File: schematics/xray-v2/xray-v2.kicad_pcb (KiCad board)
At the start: 4 copper layers, 144 x 69 mm, 136 parts, among them J1 USB_B_Micro, J2 USB_A, J3 USB_C_Receptacle_USB2.0, J4 USBASP, J5 USB_B_Micro, M1 VibroMotor, 3V, 8x2.7mm, Q1 IRF7832PbF, Q10 IRLML5203, Q11 IRLML0030, Q12 IRLML0030, Q13 IRLML0030, Q14 IRLML0030, Q2 IRF7425PbF, Q3 IRLML0030, Q4 IRF7425PbF, Q5 IRLML5203, Q6 IRLML5203, Q7 BC847, Q8 IRLML0030, Q9 IRLML5203, SW1 EC11W****, SW2 B3F3150, SW3 SW_Push, T1 Transformer_1P_1S, U1 PCA9306, U2 IP5328P, U3 ATmega328P-A, U4 SN74LVC2T45DCUR, U5 SN74LVC2T45DCUR, U6 SN74LVC2T45DCUR, U7 Display_1.18inch_st7535, U8 AMS1117-3.3, U9 CP2102N-Axx-xQFN28, Y1 HC-49SM, 8MHz

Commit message: Display changed 1.8'' -> 2.2''
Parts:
- D3, JP1, R17, SW3: moved to B.Cu
- U7: value Display_1.18inch_st7535 -> Display_2.2inch_ili9341; footprint Library:Display_1.18inch_st7735 -> Library:Display_2.2inch_ili9341
- moved H7 24.7 mm to (85.6, 50.5)
- moved D3 11.9 mm to (142.6, 75.3)
- moved U7 7.64 mm to (100.1, 134.2)
- moved R17 0.91 mm to (121.4, 67.3)
- moved JP1 0.81 mm to (128.6, 68.1), turned to -90 degrees
- moved SW3 0.46 mm to (114.2, 67.9), turned to 90 degrees
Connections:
- U7 pad 1: GND -> Net-(Q10-D)
- U7 pad 2: Net-(Q10-D) -> GND
- U7 pad 3: TFT_DC -> GND
- U7 pad 4: MOSI -> Net-(Q10-D)
- U7 pad 5: SCK -> TFT_DC
- U7 pad 6: unconnected-(U7-NC-Pad6) -> MOSI
- U7 pad 7: unconnected-(U7-NC-Pad7) -> SCK
- U7 pad 8: unconnected-(U7-NC-Pad8) -> Net-(Q10-D)
- U7 pad 9: GND -> MISO
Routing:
- net MISO: track 6.86 -> 48.9 mm
- net Net-(Q10-D): track 29.7 -> 44.3 mm, vias 0 -> 1
- net Net-(D2-K): track 39.0 -> 27.5 mm
- net TFT_DC: track 67.3 -> 59.1 mm
- net SCK: track 64.9 -> 57.9 mm
- net MOSI: track 73.4 -> 68.4 mm
- net Net-(JP1-B): track 3.45 -> 4.11 mm, vias 1 -> 0

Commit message: Gerber files exported for a new display
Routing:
- net MOSI: track 68.4 -> 67.0 mm
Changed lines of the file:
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@@
   (segment (start 171.1 101.475) (end 171.975 101.475) (width 0.5) (layer "B.Cu") (net 32))
   (segment (start 171.975 101.475) (end 173 102.5) (width 0.5) (layer "B.Cu") (net 32))
-  (segment (start 160.332232 128.9) (end 156.7 128.9) (width 0.5) (layer "F.Cu") (net 33))
+  (segment (start 150.6 131.6) (end 147.7 131.6) (width 0.5) (layer "F.Cu") (net 33))
+  (segment (start 166.6 122.632232) (end 159.432232 129.8) (width 0.5) (layer "F.Cu") (net 33))
+  (segment (start 152.4 129.8) (end 150.6 131.6) (width 0.5) (layer "F.Cu") (net 33))
   (segment (start 166.6 121) (end 166.6 122.632232) (width 0.5) (layer "F.Cu") (net 33))
-  (segment (start 166.6 122.632232) (end 160.332232 128.9) (width 0.5) (layer "F.Cu") (net 33))
   (segment (start 144.5625 125.15) (end 144.5625 125.676104) (width 0.2) (layer "F.Cu") (net 33))
-  (segment (start 156.7 128.9) (end 155.6 130) (width 0.5) (layer "F.Cu") (net 33))
   (segment (start 146.85 127.963604) (end 146.85 130.75) (width 0.2) (layer "F.Cu") (net 33))
-  (segment (start 151.4 130) (end 149.8 131.6) (width 0.5) (layer "F.Cu") (net 33))
+  (segment (start 159.432232 129.8) (end 152.4 129.8) (width 0.5) (layer "F.Cu") (net 33))
   (segment (start 144.5625 125.676104) (end 146.85 127.963604) (width 0.2) (layer "F.Cu") (net 33))
-  (segment (start 155.6 130) (end 151.4 130) (width 0.5) (layer "F.Cu") (net 33))
-  (segment (start 149.8 131.6) (end 147.7 131.6) (width 0.5) (layer "F.Cu") (net 33))
   (segment (start 146.85 130.75) (end 147.7 131.6) (width 0.2) (layer "F.Cu") (net 33))
   (segment (start 147.4 127.0875) (end 147.4 131.3) (width 0.2) (layer "B.Cu") (net 33))
@@
   (segment (start 171.8 109.3) (end 173.7 111.2) (width 0.2) (layer "In2.Cu") (net 89))
   (segment (start 184.28649 111.2) (end 184.293245 111.206755) (width 0.2) (layer "In2.Cu") (net 89))
+  (segment (start 167.410051 122.6) (end 156.61005 133.4) (width 0.2) (layer "F.Cu") (net 95))
+  (segment (start 139 129.6) (end 124.1 129.6) (width 0.2) (layer "F.Cu") (net 95))
+  (segment (start 169.8 121) (end 169.8 119.7) (width 0.2) (layer "F.Cu") (net 95))
   (segment (start 169.8 122.175) (end 169.375 122.6) (width 0.2) (layer "F.Cu") (net 95))
-  (segment (start 140 132.5) (end 140 130.6) (width 0.2) (layer "F.Cu") (net 95))
-  (segment (start 169.8 121) (end 169.8 119.7) (width 0.2) (layer "F.Cu") (net 95))
+  (segment (start 156.61005 133.4) (end 142.8 133.4) (width 0.2) (layer "F.Cu") (net 95))
+  (segment (start 169.8 119.7) (end 170.25 119.25) (width 0.2) (layer "F.Cu") (net 95))
+  (segment (start 142.8 133.4) (end 139 129.6) (width 0.2) (layer "F.Cu") (net 95))
+  (segment (start 169.375 122.6) (end 167.410051 122.6) (width 0.2) (layer "F.Cu") (net 95))
   (segment (start 169.8 121) (end 169.8 122.175) (width 0.2) (layer "F.Cu") (net 95))
-  (segment (start 167.410051 122.6) (end 156.61005 133.4) (width 0.2) (layer "F.Cu") (net 95))
-  (segment (start 140 130.6) (end 138.7 129.3) (width 0.2) (layer "F.Cu") (net 95))
-  (segment (start 169.375 122.6) (end 167.410051 122.6) (width 0.2) (layer "F.Cu") (net 95))
-  (segment (start 138.7 129.3) (end 124.4 129.3) (width 0.2) (layer "F.Cu") (net 95))
-  (segment (start 140.9 133.4) (end 140 132.5) (width 0.2) (layer "F.Cu") (net 95))
+  (segment (start 124.1 129.6) (end 122.3 131.4) (width 0.2) (layer "F.Cu") (net 95))
   (segment (start 122.3 131.4) (end 122.3 132.7) (width 0.2) (layer "F.Cu") (net 95))
-  (segment (start 124.4 129.3) (end 122.3 131.4) (width 0.2) (layer "F.Cu") (net 95))
-  (segment (start 169.8 119.7) (end 170.25 119.25) (width 0.2) (layer "F.Cu") (net 95))
-  (segment (start 156.61005 133.4) (end 140.9 133.4) (width 0.2) (layer "F.Cu") (net 95))
   (via (at 174.5 122.75) (size 0.8) (drill 0.4) (layers "F.Cu" "B.Cu") (net 95))
   (via (at 170.25 119.25) (size 0.8) (drill 0.4) (layers "F.Cu" "B.Cu") (net 95))

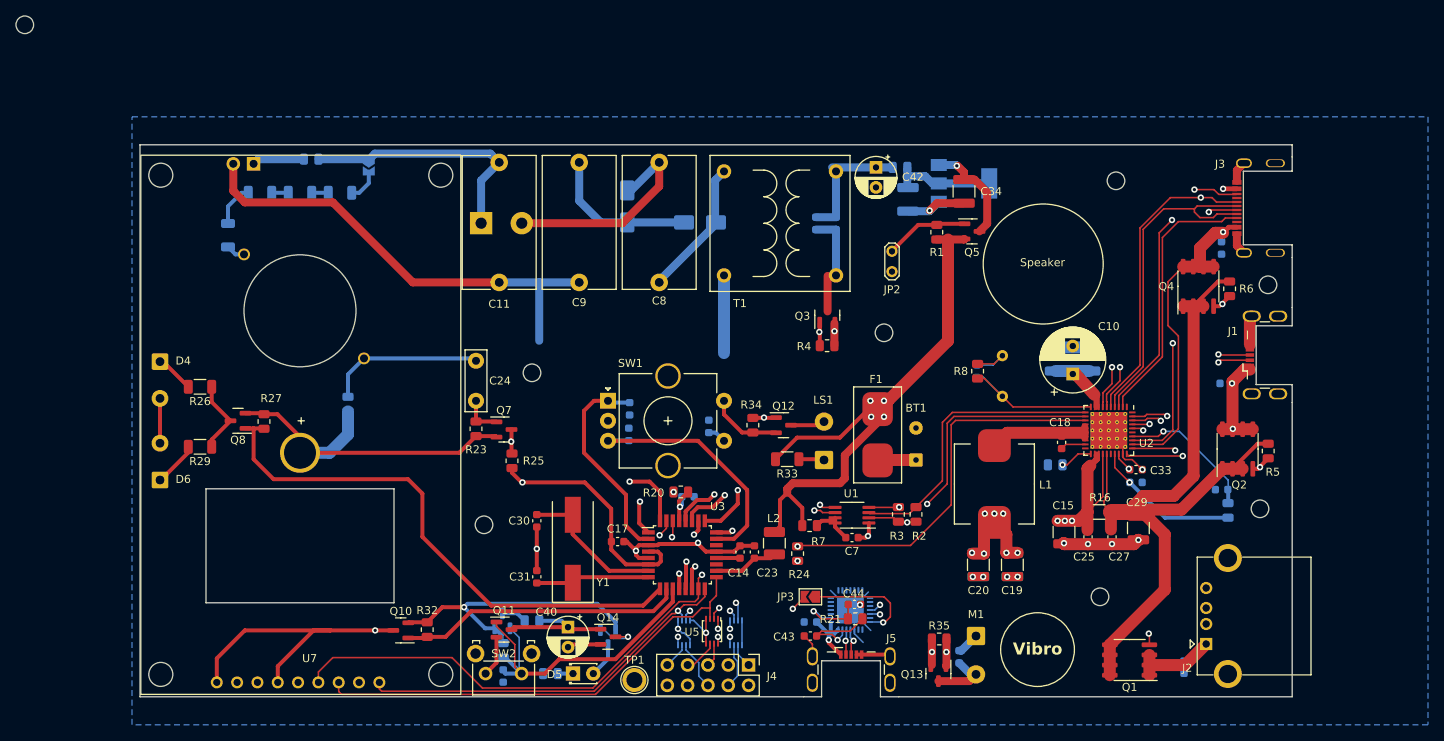
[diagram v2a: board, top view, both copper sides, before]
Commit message: changed usb-flush schematics
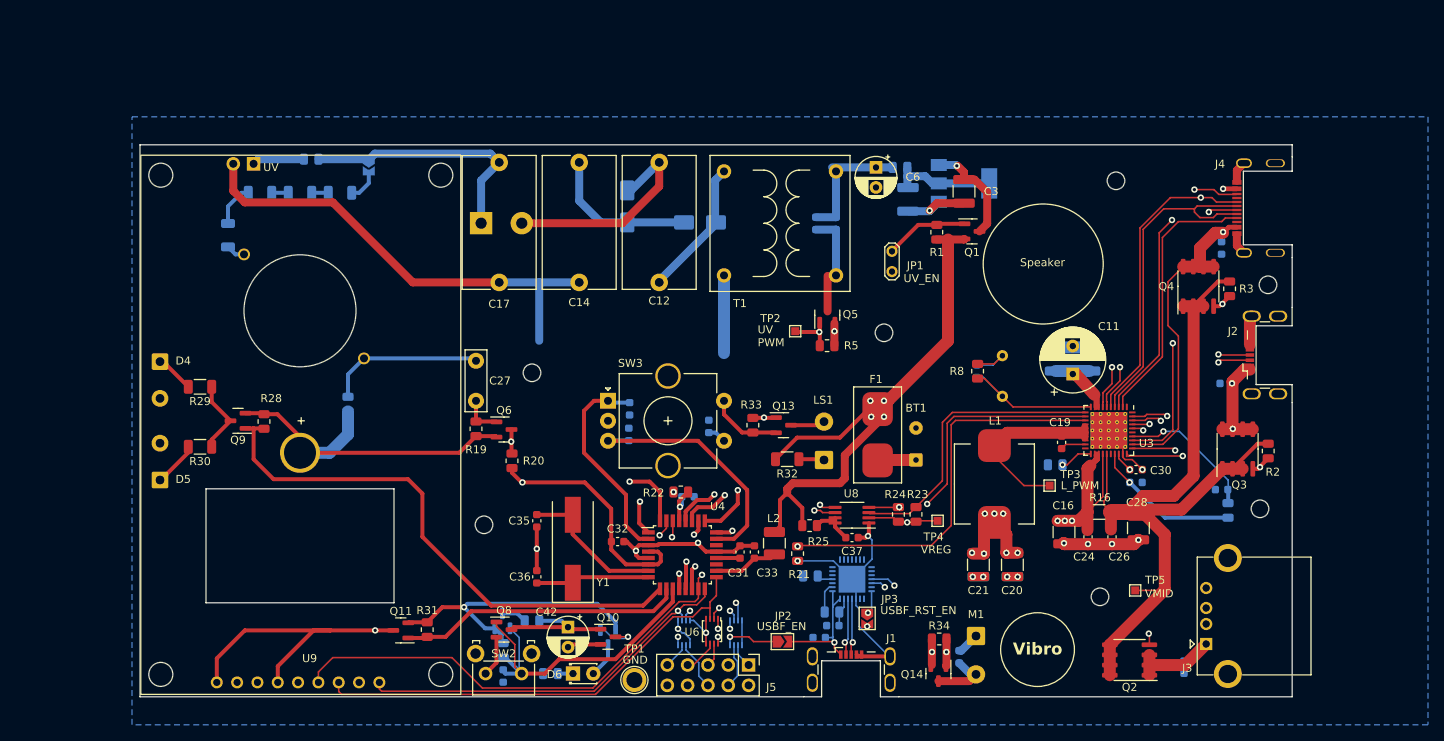
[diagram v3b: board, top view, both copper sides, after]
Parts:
- removed C44: 100 nF, Capacitor_SMD:C_0603_1608Metric
- removed the H7 at (85.6, 50.5)
- added JP2: USBF_EN, Jumper:SolderJumper-2_P1.3mm_Open_TrianglePad1.0x1.5mm, F.Cu at (180.3, 127.6)
- added R7: 10K, Resistor_SMD:R_0805_2012Metric, B.Cu at (183.8, 119.4)
- added TP2: UV_PWM, TestPoint:TestPoint_Pad_1.0x1.0mm, F.Cu at (181.9, 88.8)
- added TP3: L_PWM, TestPoint:TestPoint_Pad_1.0x1.0mm, F.Cu at (213.7, 108.1)
- added TP4: VREG, TestPoint:TestPoint_Pad_1.0x1.0mm, F.Cu at (199.7, 112.5)
- added TP5: VMID, TestPoint:TestPoint_Pad_1.0x1.0mm, F.Cu at (224.4, 121.2)
- C10: renamed from C43; moved to B.Cu
- JP1: renamed from JP2; value Jumper_2_Open -> UV_EN
- JP3: value SolderJumper_2_Open -> USBF_RST_EN
- R6: renamed from R21; value 10K -> 1K; moved to B.Cu
- moved JP3 7.60 mm to (190.9, 124.7), turned to -90 degrees
- moved U2 3.86 mm to (189.0, 119.8)
- moved C10 3.09 mm to (186.6, 125.6)
- moved R6 3.02 mm to (186.5, 123.9)
- moved C8 2.24 mm to (184.9, 127.1)
- renumbered C2 to C1, C10 to C11, C8 to C12, C12 to C13, C9 to C14, C13 to C15, C15 to C16, C11 to C17, C16 to C18, C18 to C19, C3 to C2, C19 to C20, C20 to C21, C21 to C22, C22 to C23, C25 to C24, C26 to C25, C27 to C26, C24 to C27, C29 to C28, C32 to C29, C34 to C3, C33 to C30, C14 to C31, C17 to C32, C23 to C33, C28 to C34, C30 to C35, C31 to C36, C7 to C37, C35 to C39, C36 to C40, C37 to C41, C40 to C42, C39 to C43, C41 to C5, C42 to C6, C5 to C7, C1 to C8, C6 to C9, D6 to D5, D5 to D6, H8 to H7, J5 to J1, J1 to J2, J2 to J3, J3 to J4, J4 to J5, JP1 to JP4, Q5 to Q1, Q14 to Q10, Q10 to Q11, Q6 to Q12, Q12 to Q13, Q13 to Q14, Q1 to Q2, Q2 to Q3, Q3 to Q5, Q7 to Q6, Q9 to Q7, Q11 to Q8, Q8 to Q9, R17 to R10, R10 to R11, R11 to R12, R12 to R13, R15 to R14, R13 to R15, R14 to R17, R19 to R18, R23 to R19, R5 to R2, R25 to R20, R24 to R21, R20 to R22, R2 to R23, R3 to R24, R7 to R25, R30 to R26, R31 to R27, R27 to R28, R26 to R29, R6 to R3, R29 to R30, R32 to R31, R33 to R32, R34 to R33, R35 to R34, R22 to R35, R18 to R4, R4 to R5, SW3 to SW1, SW1 to SW3, U8 to U1, U9 to U2, U2 to U3, U3 to U4, U4 to U5, U5 to U6, U6 to U7, U1 to U8, U7 to U9, V2 to V1
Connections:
- J5 pad 4: Net-(J4-Pin_4) -> RXD_5V
- J5 pad 6: Net-(J4-Pin_6) -> TXD_5V
- U2 pad 11: unconnected-(U9-~{SUSPEND}-Pad11) -> Net-(U2-~{SUSPEND})
- U2 pad 25: TXD -> TXD_5V
- U2 pad 26: RXD -> RXD_5V
- U5 pad 7: Net-(J4-Pin_4) -> RXD_5V
- U7 pad 6: Net-(J4-Pin_6) -> TXD_5V
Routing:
- net TXD_5V: track 0.00 -> 41.8 mm, vias 0 -> 1
- net RXD_5V: track 0.00 -> 37.5 mm, vias 0 -> 1
- net TXD: track 43.0 -> 14.6 mm, vias 3 -> 2
- net RXD: track 42.9 -> 17.3 mm, vias 3 -> 2
- net Net-(JP3-A): track 14.2 -> 2.94 mm
- net Net-(U3-LX_1): track 13.1 -> 21.5 mm
- net GND: track 237.1 -> 245.4 mm, vias 19 -> 18
- net FLUSH_VBUS: track 8.27 -> 16.4 mm
- net CP2102_VREG: track 10.9 -> 3.53 mm, vias 1 -> 0
- net RESET: track 55.7 -> 63.1 mm
- net Net-(J4-Pin_6): track 6.15 -> 0.00 mm
- net +5V: track 17.2 -> 23.2 mm
- net Net-(J4-Pin_4): track 5.67 -> 0.00 mm
- net Net-(U2-~{RST}): track 8.95 -> 3.74 mm, vias 1 -> 0
- net FLUSH_D-: track 3.18 -> 7.29 mm
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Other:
- board text added: "UV"
- board text added: "UV DIS"
- board text added: "UV OUT"
- board text added: "UV PWM"
